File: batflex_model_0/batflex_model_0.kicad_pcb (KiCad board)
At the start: 2 copper layers, 47.8 x 8.1 mm, 7 parts, among them J1 Conn_02x04_Odd_Even

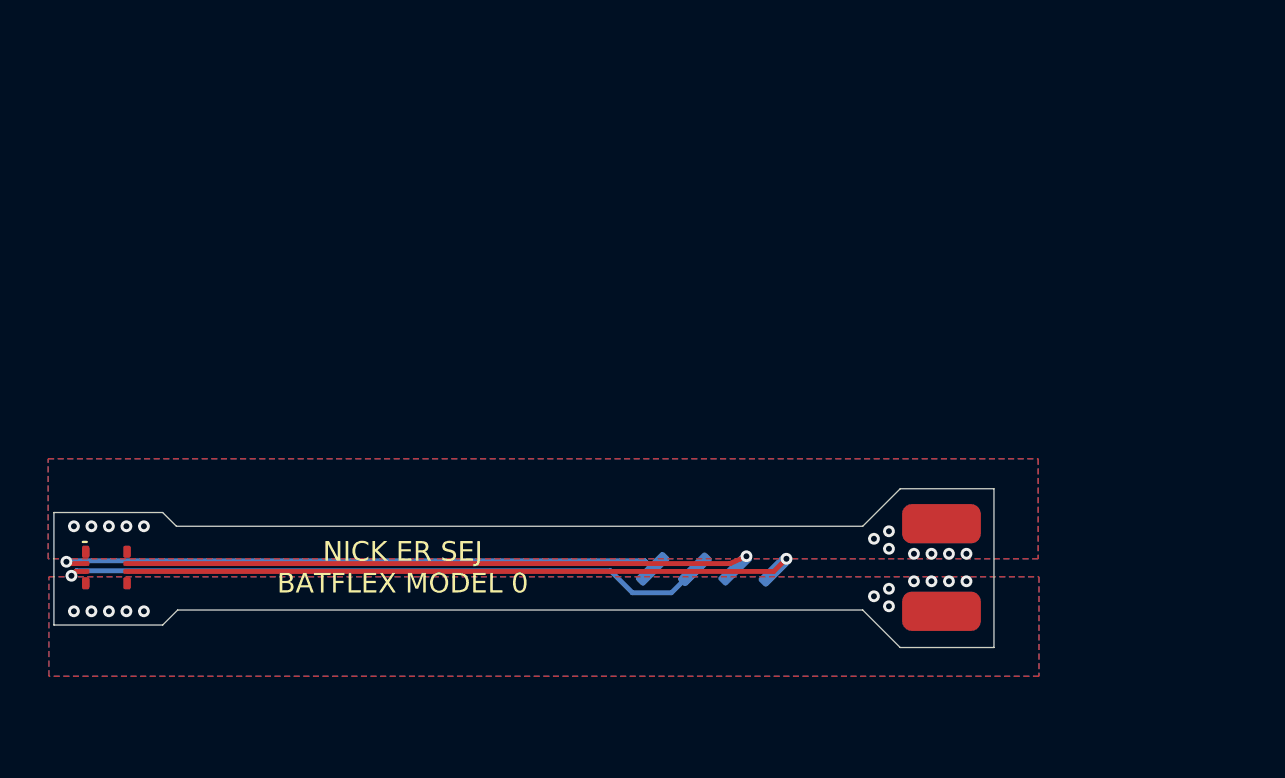
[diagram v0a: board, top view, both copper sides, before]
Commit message: Add footprints to resistors...
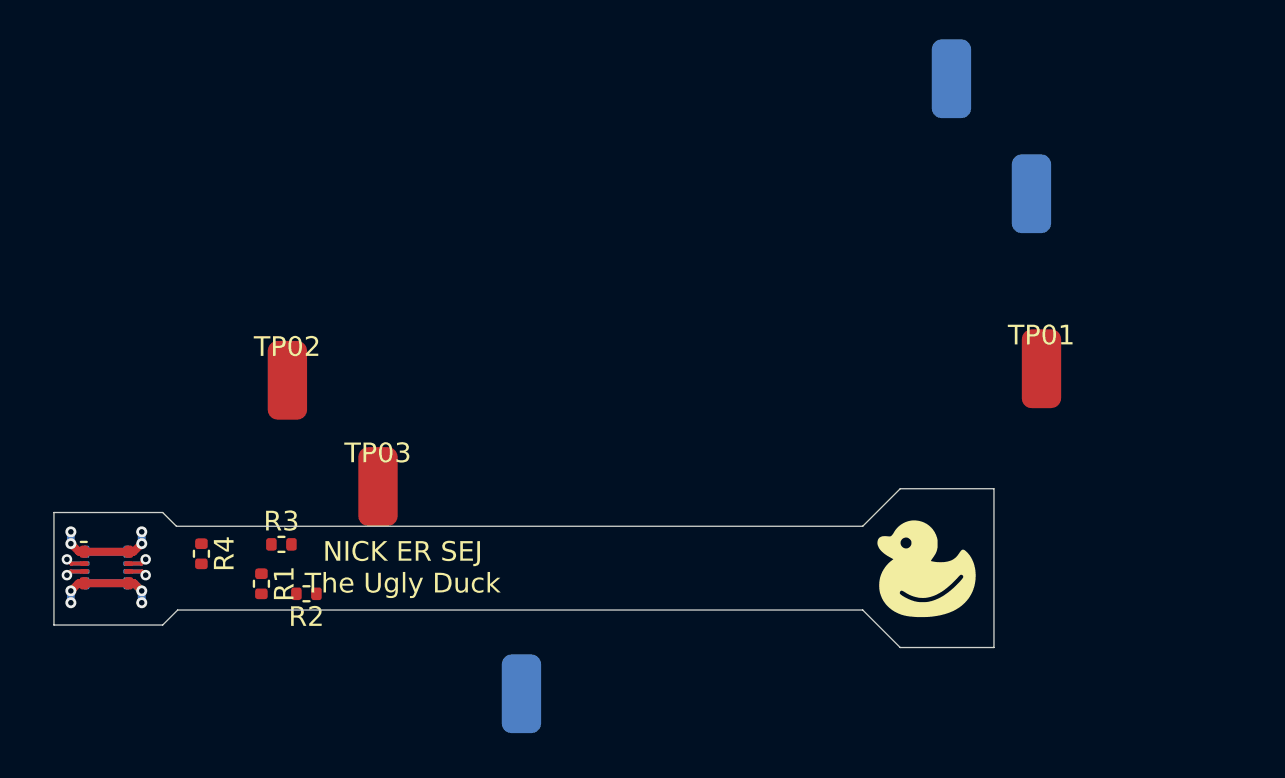
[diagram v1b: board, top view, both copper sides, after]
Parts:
- removed TP1, TP2, TP3, TP4: TestPoint, batflex:wire_pad_0.6x2mm
- removed TP5, TP6: TestPoint, batflex:wire_pad_2x4mm
- added G***: LOGO, LOGO, F.Cu at (191.3, 100.1)
- added J2: molex_505006, batflex:molex_5050060812, B.Cu at (149.6, 100.0)
- added R1: 1K, Resistor_SMD:R_0402_1005Metric, F.Cu at (157.5, 100.8)
- added R2: 1K, Resistor_SMD:R_0402_1005Metric, F.Cu at (159.8, 101.3)
- added R3: 1K, Resistor_SMD:R_0402_1005Metric, F.Cu at (158.5, 98.8)
- added R4: 1K, Resistor_SMD:R_0402_1005Metric, F.Cu at (154.4, 99.3)
- added TP01: GND, batflex:wire_pad_2x4mm, F.Cu at (197.1, 89.9)
- added TP02: V_BATT_PCB, batflex:wire_pad_2x4mm, F.Cu at (158.8, 90.5)
- added TP03: V_BATT, batflex:wire_pad_2x4mm, F.Cu at (163.4, 95.9)
- added TP10: GND, batflex:wire_pad_2x4mm, B.Cu at (170.7, 106.4)
- added TP20: V_BATT, batflex:wire_pad_2x4mm, B.Cu at (196.6, 81.0)
- added TP30: V_BATT_PCB, batflex:wire_pad_2x4mm, B.Cu at (192.5, 75.2)
- J1: value Conn_02x04_Odd_Even -> molex_505004; footprint batflex:molex_5050060812 -> batflex:molex_5050040812
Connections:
- net +BATT renamed Net-(J1-Pad1)
- net GND renamed Net-(J1-Pad7)
- J1 pad 3: /A -> /B
- J1 pad 4: /C -> /D
- J1 pad 5: /B -> /A
- J1 pad 6: /D -> /C
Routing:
- net /D: track 33.8 -> 1.98 mm
- net /B: track 33.6 -> 2.03 mm
- net /C: track 31.5 -> 1.96 mm
- net /A: track 31.0 -> 1.99 mm
- net Net-(J1-Pad7): track 0.00 -> 8.18 mm, vias 12 -> 4
- net Net-(J1-Pad1): track 0.00 -> 5.16 mm, vias 12 -> 4
- net Net-(J2-Pad7): track 0.00 -> 2.10 mm
- removed copper zone on B.Cu, net Net-(J1-Pad1)
- removed copper zone on F.Cu, net Net-(J1-Pad1)
- removed copper zone on B.Cu, net Net-(J1-Pad7)
- removed copper zone on F.Cu, net Net-(J1-Pad7)
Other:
- net class Default removed
- board text added: "NICK ER SEJ The Ugly Duck"
- board text removed: "DO NOT MANUFACUTRE THIS"
- board text removed: "NICK ER SEJ BATFLEX MODEL 0"
- board text removed: "THIS IS A DESIGN SKETCH ONLY"

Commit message: First iteration of layout wiht 0402 resistors
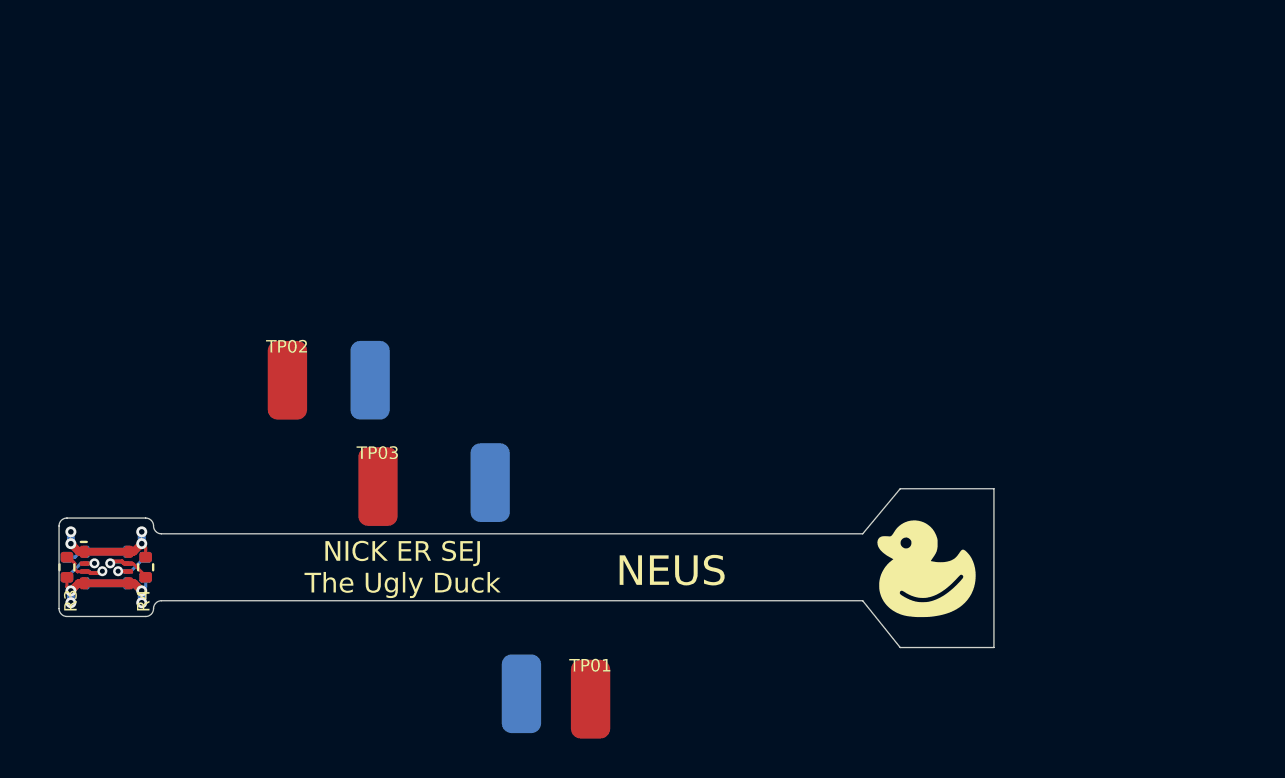
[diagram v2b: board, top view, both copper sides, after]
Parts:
- R1, R2: moved to B.Cu
- moved TP20 34.9 mm to (163.0, 90.5)
- moved TP30 31.1 mm to (169.1, 95.7)
- moved TP01 28.4 mm to (174.2, 106.7)
- moved R3 11.0 mm to (147.6, 100.0), turned to 90 degrees
- moved R1 9.92 mm to (147.6, 100.0)
- moved R2 8.28 mm to (151.6, 100.0), turned to 90 degrees
- moved R4 2.91 mm to (151.6, 100.0)
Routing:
- net /A: track 1.99 -> 3.66 mm
- net Net-(J1-Pad7): track 8.18 -> 9.72 mm
- net /D: track 1.98 -> 3.13 mm
- net Net-(J2-Pad7): track 2.10 -> 3.17 mm
- net Net-(J1-Pad1): track 5.16 -> 5.93 mm
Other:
- board size 47.8 x 8.1 mm -> 47.5 x 8.1 mm
- board text added: "DO NOT MANUFACTURE"
- board text added: "NEUS"
- board text added: "ORANGE"

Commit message: Almost final design, TODO, fix duck, add clamps diodes
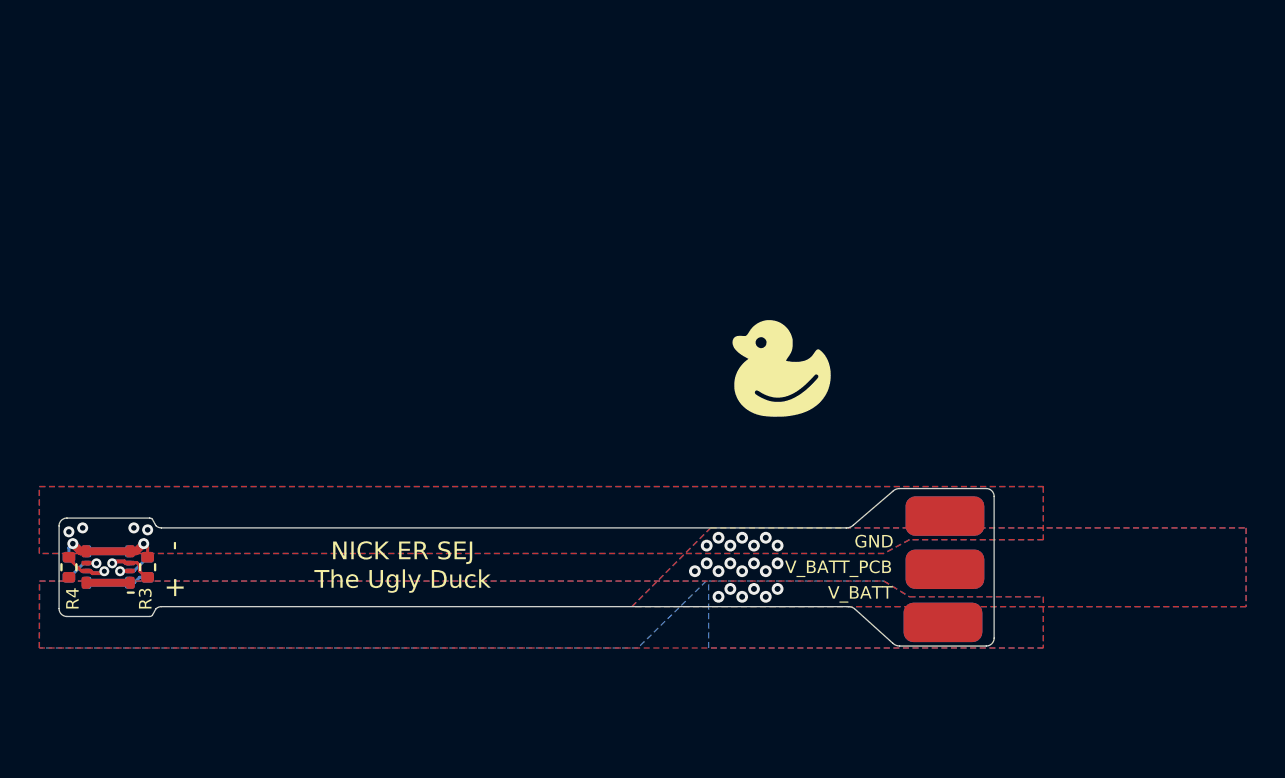
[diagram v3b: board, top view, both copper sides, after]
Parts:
- moved TP02 34.8 mm to (192.2, 100.1), turned to 90 degrees
- moved TP20 30.7 mm to (192.2, 100.1), turned to -90 degrees
- moved TP03 29.5 mm to (192.1, 102.8), turned to 90 degrees
- moved TP30 24.1 mm to (192.1, 102.8), turned to -90 degrees
- moved TP10 23.3 mm to (192.2, 97.4), turned to 90 degrees
- moved TP01 20.3 mm to (192.2, 97.4), turned to -90 degrees
- moved G*** 12.6 mm to (183.9, 89.9)
- moved R1 4.10 mm to (151.7, 100.0), turned to 90 degrees
- moved R3 4.10 mm to (151.7, 100.0), turned to -90 degrees
- moved R2 3.90 mm to (147.7, 100.0), turned to -90 degrees
- moved R4 3.90 mm to (147.7, 100.0), turned to 90 degrees
- moved J1 0.09 mm to (149.7, 100.0), turned to 180 degrees
- moved J2 0.09 mm to (149.7, 100.0), turned to 180 degrees
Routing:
- net Net-(J1-Pad1): track 5.93 -> 2.27 mm, vias 4 -> 6
- net Net-(J1-Pad7): track 9.72 -> 8.52 mm, vias 4 -> 13
- net Net-(J2-Pad7): vias 0 -> 8
- added copper zone on B.Cu, net Net-(J1-Pad1)
- added copper zone on F.Cu, net Net-(J1-Pad1)
- added copper zone on B.Cu, net Net-(J1-Pad7)
- added copper zone on F.Cu, net Net-(J1-Pad7)
- added copper zone on B.Cu, net Net-(J2-Pad7)
- added copper zone on F.Cu, net Net-(J2-Pad7)
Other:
- board size 47.5 x 8.1 mm -> 47.5 x 8 mm
- board text added: "+"
- board text added: "-"
- board text removed: "DO NOT MANUFACTURE"
- board text removed: "NEUS"
- board text removed: "ORANGE"

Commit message: Add protection and fix duck
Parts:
- removed the G*** at (183.9, 89.9)
- added D101: MM5Zxx, Diode_SMD:D_SOD-523, F.Cu at (174.0, 99.9)
- added D102: MM5Zxx, Diode_SMD:D_SOD-523, B.Cu at (171.7, 99.9)
- added D103: MM5Zxx, Diode_SMD:D_SOD-523, F.Cu at (176.3, 99.9)
- added D104: MM5Zxx, Diode_SMD:D_SOD-523, B.Cu at (174.0, 99.9)
- added D105: MM5Zxx, Diode_SMD:D_SOD-523, F.Cu at (171.7, 99.9)
- added D106: MM5Zxx, Diode_SMD:D_SOD-523, B.Cu at (176.3, 99.9)
- added G***: LOGO, LOGO, F.Cu at (155.7, 99.9)
- added G***: LOGO, LOGO, B.Cu at (168.7, 99.9)
- added G***: LOGO, LOGO, B.Cu at (161.1, 99.9)
- added G***: LOGO, LOGO, B.Cu at (164.9, 99.9)
- added G***: LOGO, LOGO, B.Cu at (157.2, 99.9)
- renumbered TP01 to TP1, TP02 to TP2, TP03 to TP3
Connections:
- net Net-(J1-Pad7) renamed /GND
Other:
- board text added: "NICK ER SEJ The Ugly Duck v1"
- board text removed: "NICK ER SEJ The Ugly Duck"

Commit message: Add mechanical pads to female connector
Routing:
- net /GND: vias 13 -> 11
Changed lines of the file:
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@@
       (effects (font (size 0.635 0.635) (thickness 0.1524)))
     )
-    (fp_line (start -1 -1.3) (end -1.3 -1.3) (layer "F.SilkS") (width 0.12))
-    (fp_line (start -0.15 1.16) (end -0.88 1.16) (layer "Cmts.User") (width 0.05))
-    (fp_line (start 0.15 1.16) (end 0.88 1.16) (layer "Cmts.User") (width 0.05))
-    (fp_line (start -0.88 -1.16) (end -0.88 1.16) (layer "Cmts.User") (width 0.05))
+    (fp_line (start -1.5 -0.9) (end -1.5 -1.2) (layer "F.SilkS") (width 0.12))
+    (fp_line (start -1.154 -1.2) (end -1.5 -1.2) (layer "F.SilkS") (width 0.12))
+    (fp_line (start -0.15 -1.16) (end -0.88 -1.16) (layer "Cmts.User") (width 0.05))
     (fp_line (start 0.88 1.16) (end 0.88 -1.16) (layer "Cmts.User") (width 0.05))
+    (fp_line (start -0.88 -1.16) (end -0.88 1.16) (layer "Cmts.User") (width 0.05))
     (fp_line (start -0.15 -1.16) (end -0.15 1.16) (layer "Cmts.User") (width 0.05))
-    (fp_line (start 0.15 -1.16) (end 0.88 -1.16) (layer "Cmts.User") (width 0.05))
-    (fp_line (start -0.15 -1.16) (end -0.88 -1.16) (layer "Cmts.User") (width 0.05))
+    (fp_line (start -0.15 1.16) (end -0.88 1.16) (layer "Cmts.User") (width 0.05))
     (fp_line (start 0.15 1.16) (end 0.15 -1.16) (layer "Cmts.User") (width 0.05))
-    (fp_line (start 1.25 2.1) (end 1.25 -2.1) (layer "F.CrtYd") (width 0.05))
+    (fp_line (start 0.15 -1.16) (end 0.88 -1.16) (layer "Cmts.User") (width 0.05))
+    (fp_line (start 0.15 1.16) (end 0.88 1.16) (layer "Cmts.User") (width 0.05))
     (fp_line (start 1.25 -2.1) (end -1.25 -2.1) (layer "F.CrtYd") (width 0.05))
-    (fp_line (start -1.25 2.1) (end 1.25 2.1) (layer "F.CrtYd") (width 0.05))
     (fp_line (start -1.25 -2.1) (end -1.25 2.1) (layer "F.CrtYd") (width 0.05))
+    (fp_line (start 1.25 2.1) (end 1.25 -2.1) (layer "F.CrtYd") (width 0.05))
+    (fp_line (start -1.25 2.1) (end 1.25 2.1) (layer "F.CrtYd") (width 0.05))
     (pad "1" smd roundrect (at -1.13 -0.8 270) (size 0.62 0.45) (layers "F.Cu" "F.Paste" "F.Mask") (roundrect_rratio 0.25)
       (net 3 "Net-(J1-Pad1)") (pinfunction "Pin_1"))
@@
     (pad "8" smd roundrect (at 1.13 0.8 270) (size 0.62 0.45) (layers "F.Cu" "F.Paste" "F.Mask") (roundrect_rratio 0.25)
       (net 7 "/GND") (pinfunction "Pin_8"))
+    (pad "M1" smd roundrect (at -1.205 -1.53 270) (size 0.45 0.3) (layers "F.Cu" "F.Paste" "F.Mask") (roundrect_rratio 0.25))
+    (pad "M1" smd roundrect (at 1.205 -1.53 270) (size 0.45 0.3) (layers "F.Cu" "F.Paste" "F.Mask") (roundrect_rratio 0.25))
+    (pad "M2" smd roundrect (at -1.205 1.53 270) (size 0.45 0.3) (layers "F.Cu" "F.Paste" "F.Mask") (roundrect_rratio 0.25))
+    (pad "M2" smd roundrect (at 1.205 1.53 270) (size 0.45 0.3) (layers "F.Cu" "F.Paste" "F.Mask") (roundrect_rratio 0.25))
     (model "${KIPRJMOD}/../3d/5050040812.stp"
       (offset (xyz 0 0 0))
@@
   (via blind (at 181.299993 98.900005) (size 0.6) (drill 0.3) (layers "F.Cu" "B.Cu") (net 7))
   (via blind (at 147.9 98.8) (size 0.5588) (drill 0.2794) (layers "F.Cu" "B.Cu") (net 7))
-  (via blind (at 151 98) (size 0.5588) (drill 0.2794) (layers "F.Cu" "B.Cu") (net 7))
   (via blind (at 147.7 98.2) (size 0.5588) (drill 0.2794) (layers "F.Cu" "B.Cu") (net 7))
   (via blind (at 181.899992 98.500006) (size 0.6) (drill 0.3) (layers "F.Cu" "B.Cu") (net 7))
@@
   (via blind (at 180.099995 98.900005) (size 0.6) (drill 0.3) (layers "F.Cu" "B.Cu") (net 7))
   (via blind (at 183.699988 98.900005) (size 0.6) (drill 0.3) (layers "F.Cu" "B.Cu") (net 7))
-  (via blind (at 148.4 98) (size 0.5588) (drill 0.2794) (layers "F.Cu" "B.Cu") (net 7))
   (arc (start 150.841678 99.2) (mid 150.836894 99.199048) (end 150.832839 99.196339) (width 0.4) (layer "F.Cu") (net 7))
   (arc (start 150.832839 99.196339) (mid 150.836894 99.199048) (end 150.841677 99.2) (width 0.4) (layer "F.Cu") (net 7))

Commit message: Minor tweaks
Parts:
- moved D103 0.22 mm to (176.5, 100.0)
- moved D106 0.22 mm to (176.5, 100.0)
- moved D101 0.20 mm to (174.2, 100.0)
- moved D104 0.20 mm to (174.2, 100.0)
- moved D102 0.19 mm to (171.9, 100.0)
- moved D105 0.19 mm to (171.9, 100.0)
- moved TP3 0.10 mm to (192.2, 102.8)
- moved TP30 0.10 mm to (192.2, 102.8)
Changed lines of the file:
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@@
     (property "Sheet name" "")
     (attr smd)
-    (fp_text reference "R3" (at 1.6 0.1 90) (layer "F.SilkS")
+    (fp_text reference "R3" (at 1.6 -0.2 37) (layer "F.SilkS")
       (effects (font (size 0.635 0.635) (thickness 0.1524)))
     )
@@
   )
   (module "Diode_SMD:D_SOD-523" (layer "F.Cu")
-    (at 171.726 99.926 90)
+    (at 171.9 100 90)
     (descr "http://www.diodes.com/datasheets/ap02001.pdf p.144")
     (tags "Diode SOD523")
@@
   )
   (module "Diode_SMD:D_SOD-523" (layer "F.Cu")
-    (at 176.298 99.926 90)
+    (at 176.5 100 90)
     (descr "http://www.diodes.com/datasheets/ap02001.pdf p.144")
     (tags "Diode SOD523")
@@
   )
   (module "batflex:wire_pad_2x4mm" (layer "F.Cu")
-    (at 192.1 102.8 90)
+    (at 192.2 102.8 90)
     (property "Sheet file" "/home/nickoe/batflex/batflex_model_0/batflex_model_0.kicad_sch")
     (property "Sheet name" "")
@@
       (effects (font (size 0.635 0.635) (thickness 0.1524)))
     )
-    (fp_text value "V_BATT" (at 1.5 -4.2 180) (layer "F.SilkS")
+    (fp_text value "V_BATT" (at 1.5 -4.3 180) (layer "F.SilkS")
       (effects (font (size 0.635 0.635) (thickness 0.1524)))
     )
@@
   )
   (module "Diode_SMD:D_SOD-523" (layer "F.Cu")
-    (at 174.012 99.926 90)
+    (at 174.2 100 90)
     (descr "http://www.diodes.com/datasheets/ap02001.pdf p.144")
     (tags "Diode SOD523")
@@
       (effects (font (size 0.635 0.635) (thickness 0.1524)) (justify mirror))
     )
-    (fp_text value "V_BATT" (at -0.099999 4.2 180) (layer "B.SilkS")
+    (fp_text value "V_BATT" (at -0.099999 4.3 180) (layer "B.SilkS")
       (effects (font (size 0.635 0.635) (thickness 0.1524)) (justify mirror))
     )
@@
   )
   (module "batflex:wire_pad_2x4mm" (layer "B.Cu")
-    (at 192.100001 102.8 -90)
+    (at 192.2 102.800001 -90)
     (property "Sheet file" "/home/nickoe/batflex/batflex_model_0/batflex_model_0.kicad_sch")
     (property "Sheet name" "")
@@
       (effects (font (size 0.635 0.635) (thickness 0.1524)) (justify mirror))
     )
-    (fp_text value "V_BATT_PCB" (at -1.5 5.300001 180) (layer "B.SilkS")
+    (fp_text value "V_BATT_PCB" (at -1.5 5.5 180) (layer "B.SilkS")
       (effects (font (size 0.635 0.635) (thickness 0.1524)) (justify mirror))
     )
@@
   )
   (module "Diode_SMD:D_SOD-523" (layer "B.Cu")
-    (at 176.298 99.926 90)
+    (at 176.5 100 90)
     (descr "http://www.diodes.com/datasheets/ap02001.pdf p.144")
     (tags "Diode SOD523")
@@
   )
   (module "Diode_SMD:D_SOD-523" (layer "B.Cu")
-    (at 171.726 99.926 90)
+    (at 171.9 100 90)
     (descr "http://www.diodes.com/datasheets/ap02001.pdf p.144")
     (tags "Diode SOD523")
@@
   )
   (module "Diode_SMD:D_SOD-523" (layer "B.Cu")
-    (at 174.012 99.926 90)
+    (at 174.2 100 90)
     (descr "http://www.diodes.com/datasheets/ap02001.pdf p.144")
     (tags "Diode SOD523")
